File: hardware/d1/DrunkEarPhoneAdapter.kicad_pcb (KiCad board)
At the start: 4 copper layers, 50 x 50 mm, 185 parts, among them J3 SWD, J4 UART, Q1 CSD17577Q3A, Q2 CSD17577Q3A, Q3 DMG1012T-7, SW1 SSSS811101, SW3 DSHP02TSGER, U1 CS43131-CNZR, U10 BLM15PX601SN1D, U11 TPS7A2033PDBVR, U12 TPS7A2018PDBVR, U13 TPS7A2018PDBVR, U14 BLM15PX601SN1D, U15 ESDA25P35-1U1M, U16 ESDA25P35-1U1M, U17 SN74LVC1G32DBVR, U18 TPS22917DBVR, U19 TPS22917DBVR, U2 STM32G0B1VCT6, U20 SN74AVC4T774RSVR, U21 TCA9406DCUR, U3 TS3USB221RSER, U4 TCPP03-M20, U5 TCPP03-M20, U6 ES8327, U7 TPS7A2018PDBVR, U8 TPS7A2033PDBVR, U9 TPS560430XFDBVR, X1 22.5792MHz, X3 24.576MHz

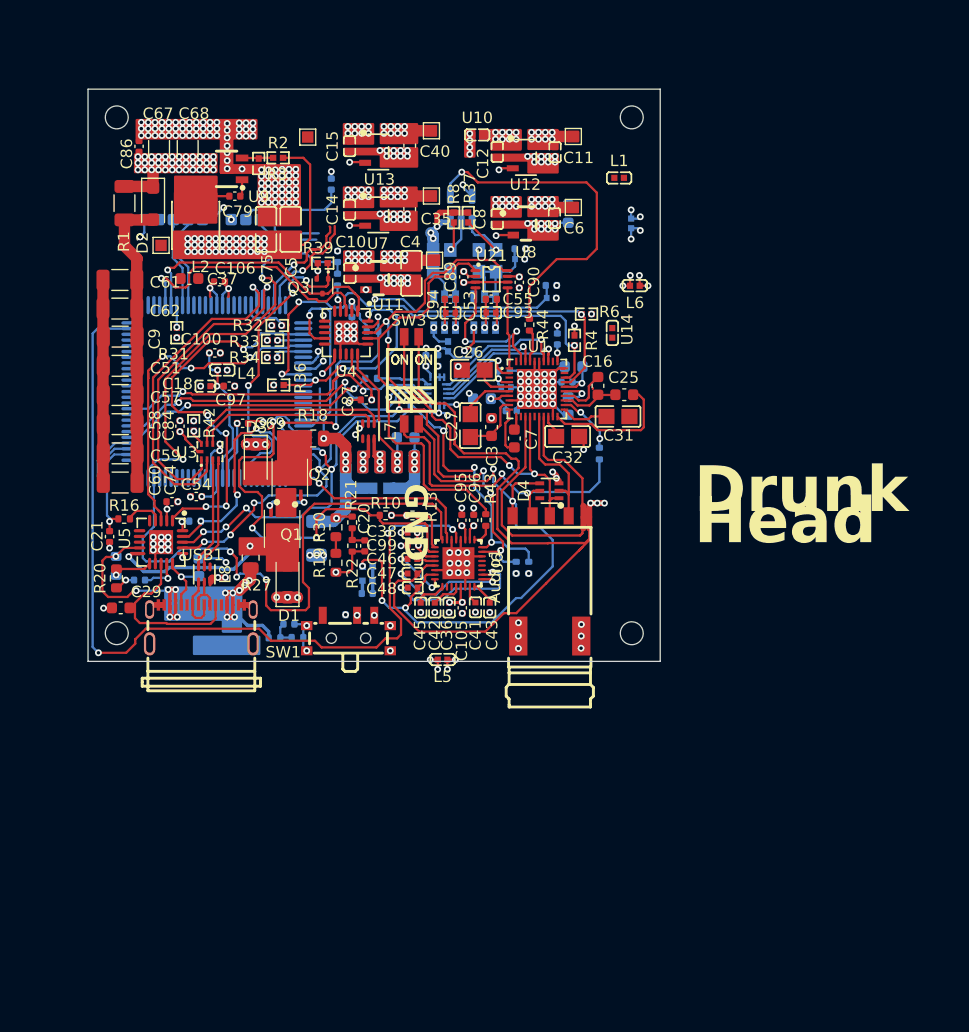
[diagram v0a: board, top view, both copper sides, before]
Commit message: Drop target, fix routes
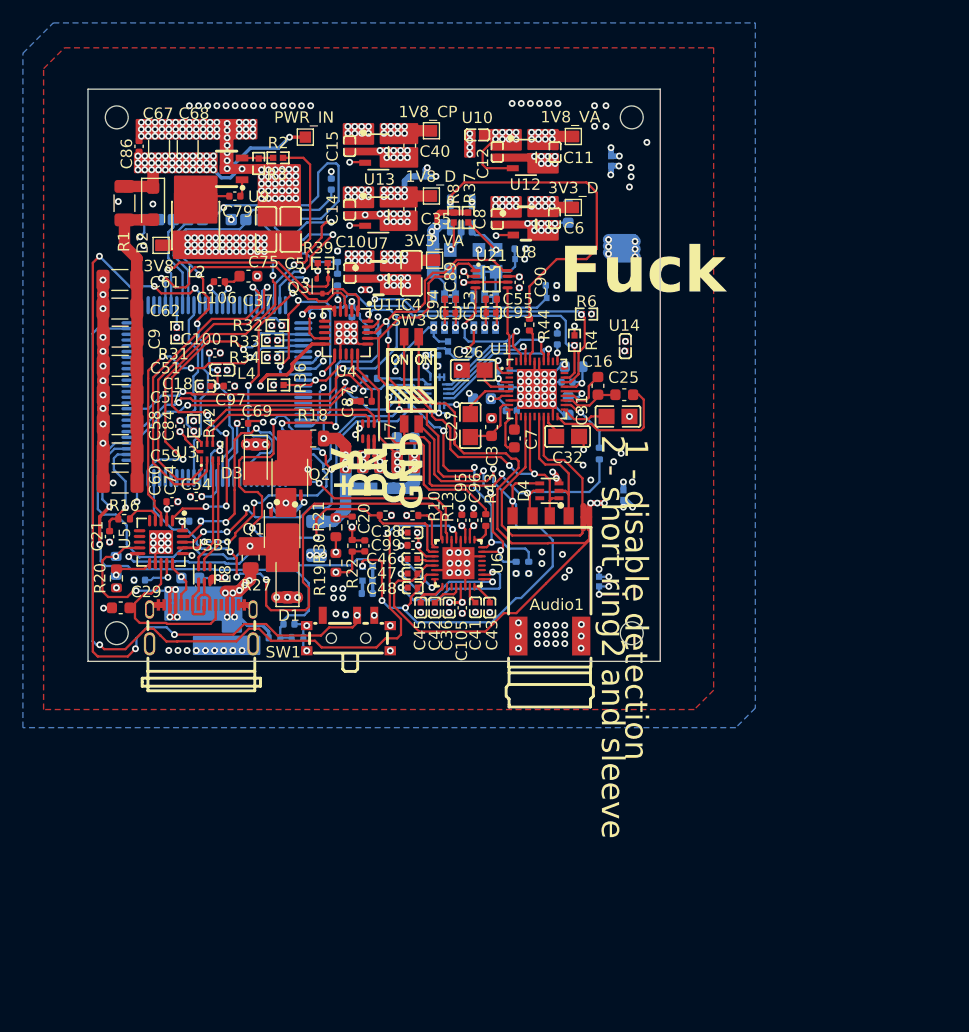
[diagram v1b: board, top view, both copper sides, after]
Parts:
- L1, L5, L6: moved to B.Cu
- USB1: value 2130830005 -> ~
- moved L3 18.8 mm to (48.4, 25.6), turned to 0 degrees
- moved L6 18.3 mm to (66.1, 53.4), turned to -90 degrees
- moved L5 15.3 mm to (64.0, 61.0), turned to 90 degrees
- moved C37 5.16 mm to (33.4, 34.3), turned to 180 degrees
- moved L1 1.63 mm to (65.0, 24.2), turned to -90 degrees
- moved U14 1.63 mm to (66.3, 40.4), turned to -90 degrees
- moved C28 1.21 mm to (28.3, 60.7), turned to 180 degrees
- moved U17 0.50 mm to (52.0, 28.9)
- moved TP7 0.21 mm to (38.3, 22.1)
- moved C87 0.12 mm to (43.6, 45.2)
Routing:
- net +3V3_D: track 30.7 -> 301.4 mm, vias 28 -> 34
- net +3V8: track 20.0 -> 136.0 mm, vias 76 -> 78
- net PWR_IN: track 9.03 -> 86.0 mm, vias 42 -> 43
- net /mcu/USB_DIR_SW: track 0.06 -> 73.4 mm, vias 1 -> 6
- net +1V8_A: track 4.56 -> 73.1 mm
- net +3V3_A: track 1.51 -> 63.4 mm
- net +1V8_D: track 8.44 -> 66.7 mm
- net +1V8_CP: track 4.55 -> 50.4 mm
- net /mcu/ADC1_IN3: track 6.15 -> 39.1 mm, vias 0 -> 2
- net /mcu/ADC1_IN4: track 7.24 -> 40.1 mm
- net Net-(U17-VCC): track 6.36 -> 38.6 mm, vias 3 -> 5
- net /mcu/NRST: track 9.61 -> 39.4 mm, vias 0 -> 2
- net Net-(U1-VD): track 5.97 -> 34.9 mm
- net /mcu/ADC1_IN1: track 2.14 -> 29.4 mm, vias 0 -> 2
- net Net-(U6-CPVDD): track 4.71 -> 31.2 mm
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- added copper zone on B.Cu, net GND
- added copper zone on F.Cu, net GND
- added copper zone on In1.Cu, net GND
- added copper zone on In2.Cu, net GND
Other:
- board text added: "+V"
- board text added: "1 - disable detection"
- board text added: "2 - short ring2 and sleeve"
- board text added: "3v3"
- board text added: "Adapter"
- board text added: "CC1"
- board text added: "CLK"
- board text added: "CTIA mic only"
- board text added: "DIO"
- board text added: "DN"
- board text added: "DP"
- board text added: "Fuck"
- board text added: "HeadPhones"
- board text added: "RST"
- board text added: "RX"
- board text added: "TX"
- board text added: "USB bypass sw"
- board text added: "Use SW3 to disable"
- board text added: "Why the fuck these braindead fuckheads"
- board text added: "github.com/drunkbatya/DrunkHeadphonesAdapter"
- board text added: "gotta ditch"
- board text added: "the headphone jack?"
- board text removed: "+3v3"
- board text removed: "Head"
- board text removed: "SWCLK"
- board text removed: "SWDIO"

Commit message: Fix track lengths
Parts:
- added TP8: GND, TestPoint:TestPoint_Pad_1.0x1.0mm, F.Cu at (40.3, 25.2)
- USB1: value ~ -> 2130830005
- moved C56 0.80 mm to (39.9, 26.7)
- moved C89 0.20 mm to (52.2, 34.6)
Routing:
- net GND: track 117.7 -> 142.2 mm, vias 344 -> 415
- net +3V8: track 136.0 -> 142.5 mm, vias 78 -> 79
- net +3V3_D: track 301.4 -> 303.9 mm, vias 34 -> 33
- net Net-(U18-QOD): track 10.5 -> 8.32 mm
- net Net-(U19-QOD): track 17.7 -> 16.0 mm
- net Net-(U1-VD): track 34.9 -> 33.3 mm
- net /adc/GMS1: track 56.1 -> 57.4 mm
- net +3V3_A: track 63.4 -> 62.2 mm, vias 10 -> 8
- net +1V8_D: track 66.7 -> 67.8 mm
- net /ucpd/VSENSE_PHONE: track 22.5 -> 23.6 mm
- net Net-(U1-VP): track 9.06 -> 10.1 mm, vias 2 -> 3
- net /mcu/NRST: track 39.4 -> 38.5 mm
- net Net-(U17-VCC): track 38.6 -> 39.2 mm
- net Net-(U2-VREF+): track 14.8 -> 15.4 mm
- net /mcu/SWDIO: track 16.4 -> 17.0 mm
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
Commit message: Fix routes
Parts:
- added C107: 100nF 50V, Capacitor_SMD:C_0402_1005Metric, B.Cu at (52.5, 26.2)
- added C108: 100nF 50V, Capacitor_SMD:C_0402_1005Metric, B.Cu at (31.6, 53.6)
- moved C77 13.2 mm to (46.6, 35.2), turned to 90 degrees
- moved C76 12.1 mm to (47.8, 35.2), turned to -90 degrees
- moved C86 6.24 mm to (30.0, 22.7)
- moved R36 0.62 mm to (36.6, 43.8)
- moved C100 0.27 mm to (30.4, 41.3)
- moved C69 0.22 mm to (33.0, 47.0)
- moved R34 0.20 mm to (35.3, 41.4)
- moved R33 0.18 mm to (35.3, 39.9)
- moved L2 0.05 mm to (28.8, 29.8)
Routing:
- net GND: track 142.2 -> 169.3 mm, vias 415 -> 398
- net /mcu/ADC1_IN1: track 29.0 -> 43.9 mm
- net +3V3_A: track 62.2 -> 47.4 mm, vias 8 -> 2
- net Net-(U17-VCC): track 39.2 -> 52.7 mm, vias 5 -> 2
- net Net-(U19-QOD): track 16.0 -> 9.92 mm
- net +3V8: track 142.5 -> 148.2 mm, vias 79 -> 52
- net +3V3_D: track 303.9 -> 309.2 mm, vias 33 -> 32
- net +1V8_D: track 67.8 -> 63.0 mm, vias 13 -> 8
- net PWR_IN: track 86.0 -> 88.8 mm, vias 43 -> 20
- net Net-(U2-VREF+): track 15.4 -> 18.1 mm
- net /ucpd/USB_CHR_VBUS: track 55.3 -> 57.6 mm
- net /dac/CLOCK_EN_24_576: track 20.4 -> 18.1 mm
- net /mcu/USB_DIR_SW: track 73.4 -> 75.4 mm
- net /dac//INT: track 43.4 -> 45.2 mm
- net Net-(U1-VP): track 10.1 -> 11.8 mm
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
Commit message: Fixes
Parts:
- C25: moved to B.Cu
- moved C56 29.8 mm to (28.5, 54.2), turned to -90 degrees
- moved C25 2.82 mm to (63.9, 46.3), turned to -90 degrees
- moved R18 0.30 mm to (38.7, 48.4)
- moved C29 0.27 mm to (22.2, 63.0)
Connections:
- L7 pad 5: /ucpd/D_P -> /ucpd/D_N
- L7 pad 6: /ucpd/D_N -> /ucpd/D_P
- USBC3 pad 2: /ucpd/D_P -> /ucpd/D_N
- USBC3 pad 3: /ucpd/D_N -> /ucpd/D_P
- USBC4 pad 2: /ucpd/D_P -> /ucpd/D_N
- USBC4 pad 3: /ucpd/D_N -> /ucpd/D_P
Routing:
- net /dac/FLYN_VCP: track 11.7 -> 5.16 mm, vias 0 -> 1
- net /mcu/NRST: track 38.5 -> 32.1 mm
- net /adc/I2S_SD: track 46.8 -> 40.9 mm
- net GND: track 169.3 -> 174.2 mm, vias 398 -> 383
- net /mcu/USB_DIR_SW: track 75.4 -> 70.7 mm
- net /ucpd/USB_CHR_VBUS: track 57.6 -> 61.3 mm, vias 13 -> 12
- net /adc/I2S_CK: track 77.1 -> 79.8 mm
- net PWR_IN: track 88.8 -> 86.7 mm, vias 20 -> 17
- net /adc/GMS1: track 58.4 -> 56.8 mm
- net /mcu/USB_DP: track 28.3 -> 29.8 mm
- net /ucpd/D_N: track 2.23 -> 3.72 mm
- net /ucpd/USB_PHONE_SAFE_DN: track 16.0 -> 17.4 mm
- net +1V8_CP: track 49.3 -> 50.8 mm
- net /dac/JACK_TIP_DETECT: track 29.6 -> 28.4 mm
- net Net-(U20-B3): track 20.8 -> 19.6 mm
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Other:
- outline, holes or cut-outs redrawn

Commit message: Fix
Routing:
- net /adc/I2S_CK: track 79.8 -> 74.2 mm
- net /mcu/USB_DIR_SW: track 70.7 -> 73.2 mm
- net /ucpd/D_N: track 3.72 -> 2.62 mm
- net GND: vias 383 -> 388
- net +3V8: vias 44 -> 41
